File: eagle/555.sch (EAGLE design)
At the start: 7 parts, among them P1 1k

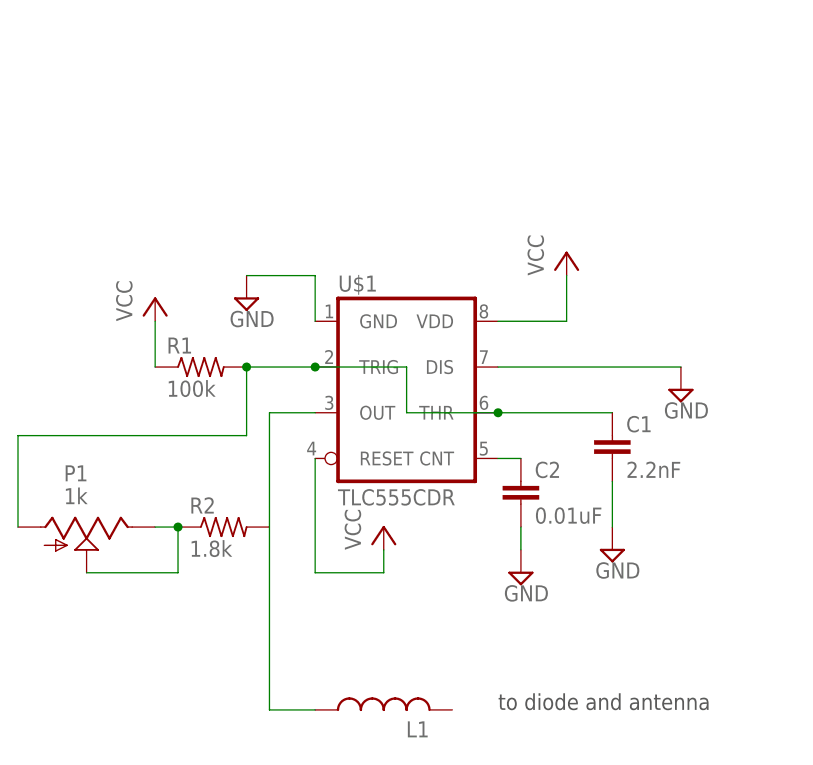
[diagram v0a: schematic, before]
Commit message: mofified 555 timer schematic and layout
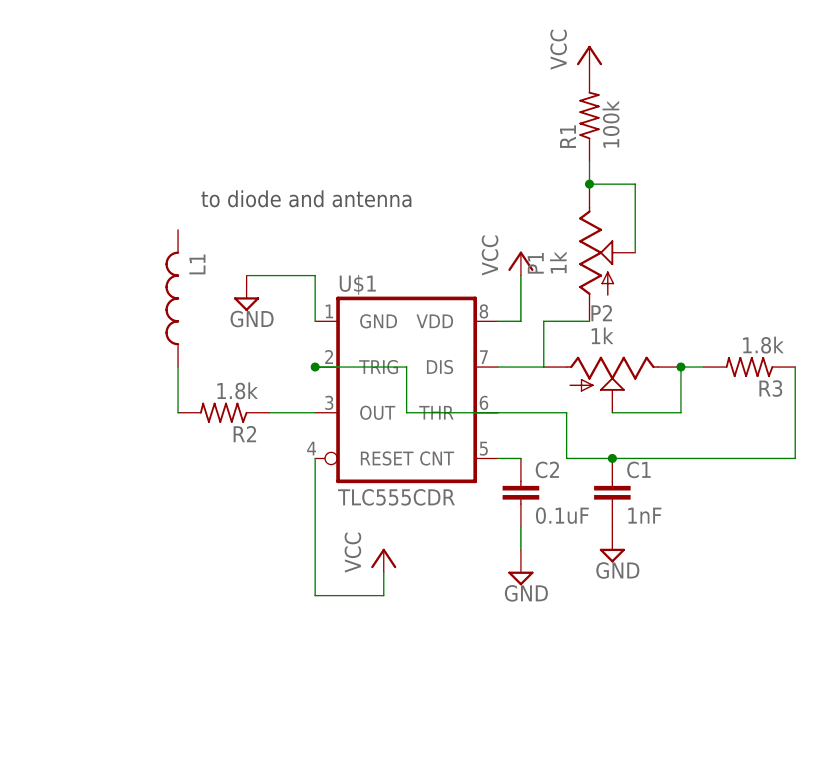
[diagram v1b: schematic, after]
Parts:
- added P2: 1k, potentiometer:TRIM_US-3223J
- added R3: 1.8k, resistor:R-US_R0805
- C1: value 2.2nF -> 1nF
- C2: value 0.01uF -> 0.1uF
- R1: device resistor:R-US_R0805 -> resistor:R-US_0204/7
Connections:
- new net N$4: C1.1, R3.1, U$1.THR, U$1.TRIG
- new net N$5: P2.E, P2.S, R3.2
- new net N$6: P1.E, R1.1
- new net N$8: L1.1, R2.2
- net GND: no longer U$1.DIS
- net N$1: now also P2.A, U$1.DIS; no longer C1.1, R1.2, U$1.THR, U$1.TRIG
- net N$2: now also R2.1; no longer L1.1, R2.2
- net N$3: no longer P1.E, R2.1
- net VCC: now also R1.2; no longer R1.1
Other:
- moved on the sheet: C1, L1, P1, R1, R2
